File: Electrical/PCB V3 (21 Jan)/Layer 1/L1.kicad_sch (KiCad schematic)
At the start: 210 parts, among them J1 Conn_01x05, U1 LM2587S-ADJ, U2 CD74HC4067SM, U3 CD74HC4067SM, U4 XT30UPB-M, U5 113991054

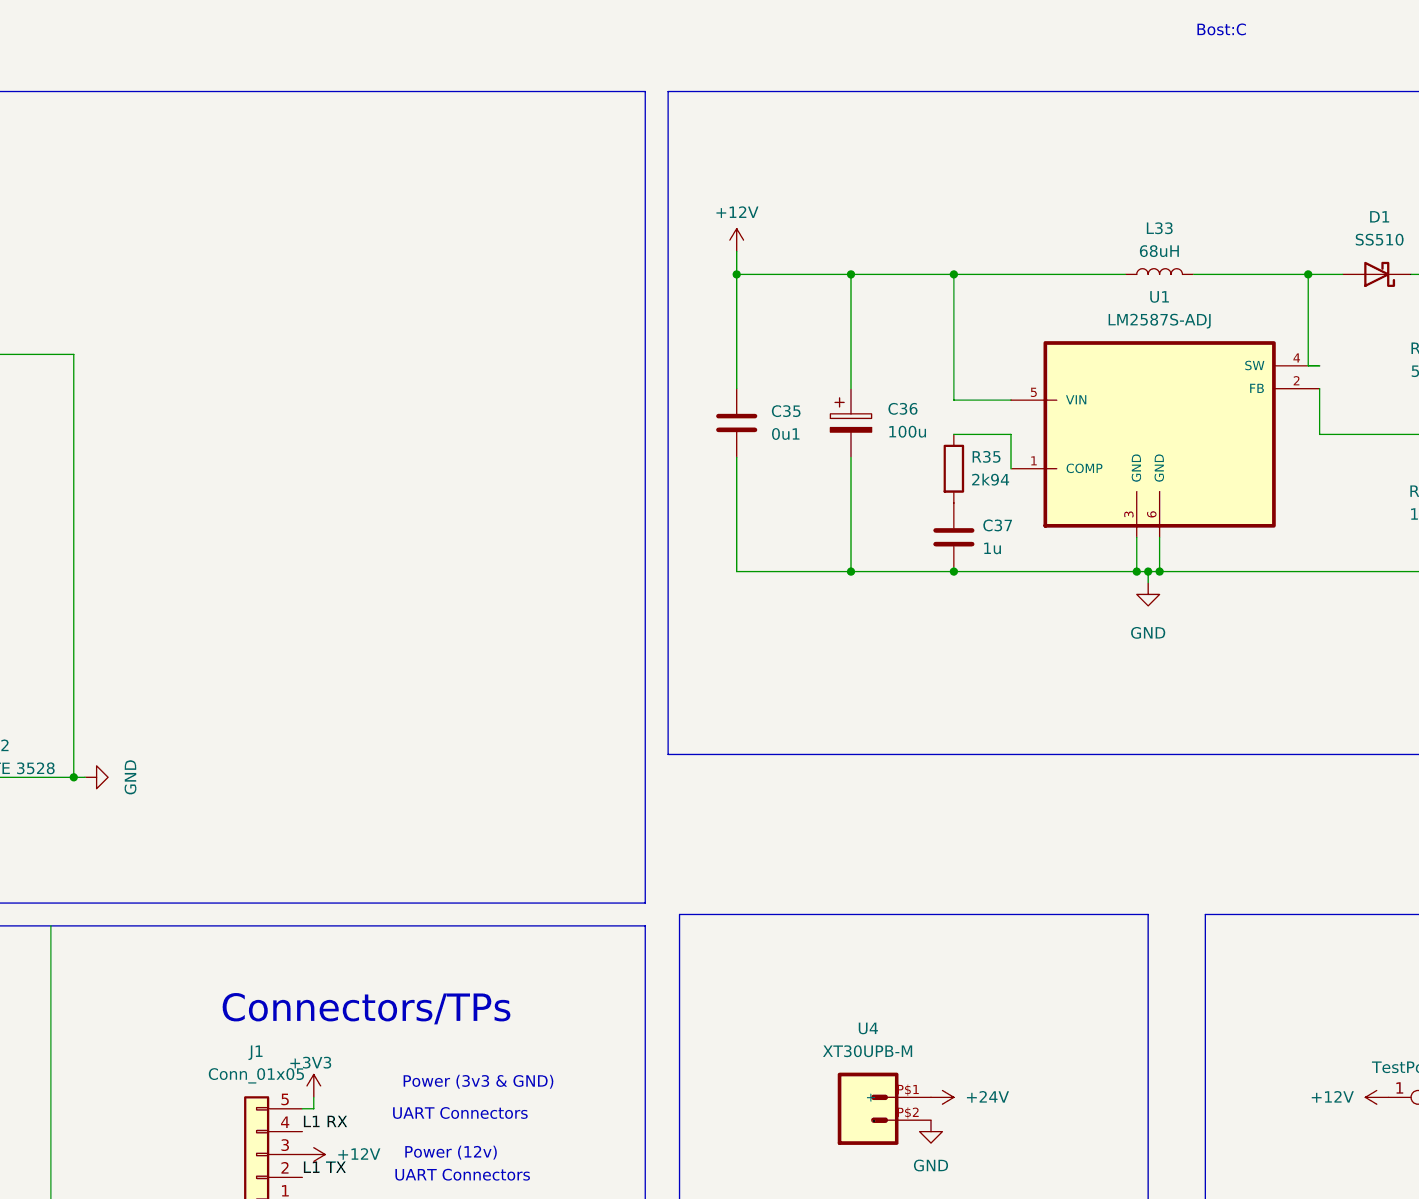
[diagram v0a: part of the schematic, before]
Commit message: redid l1 to fit new solenoid, updated l2 dxf to v6
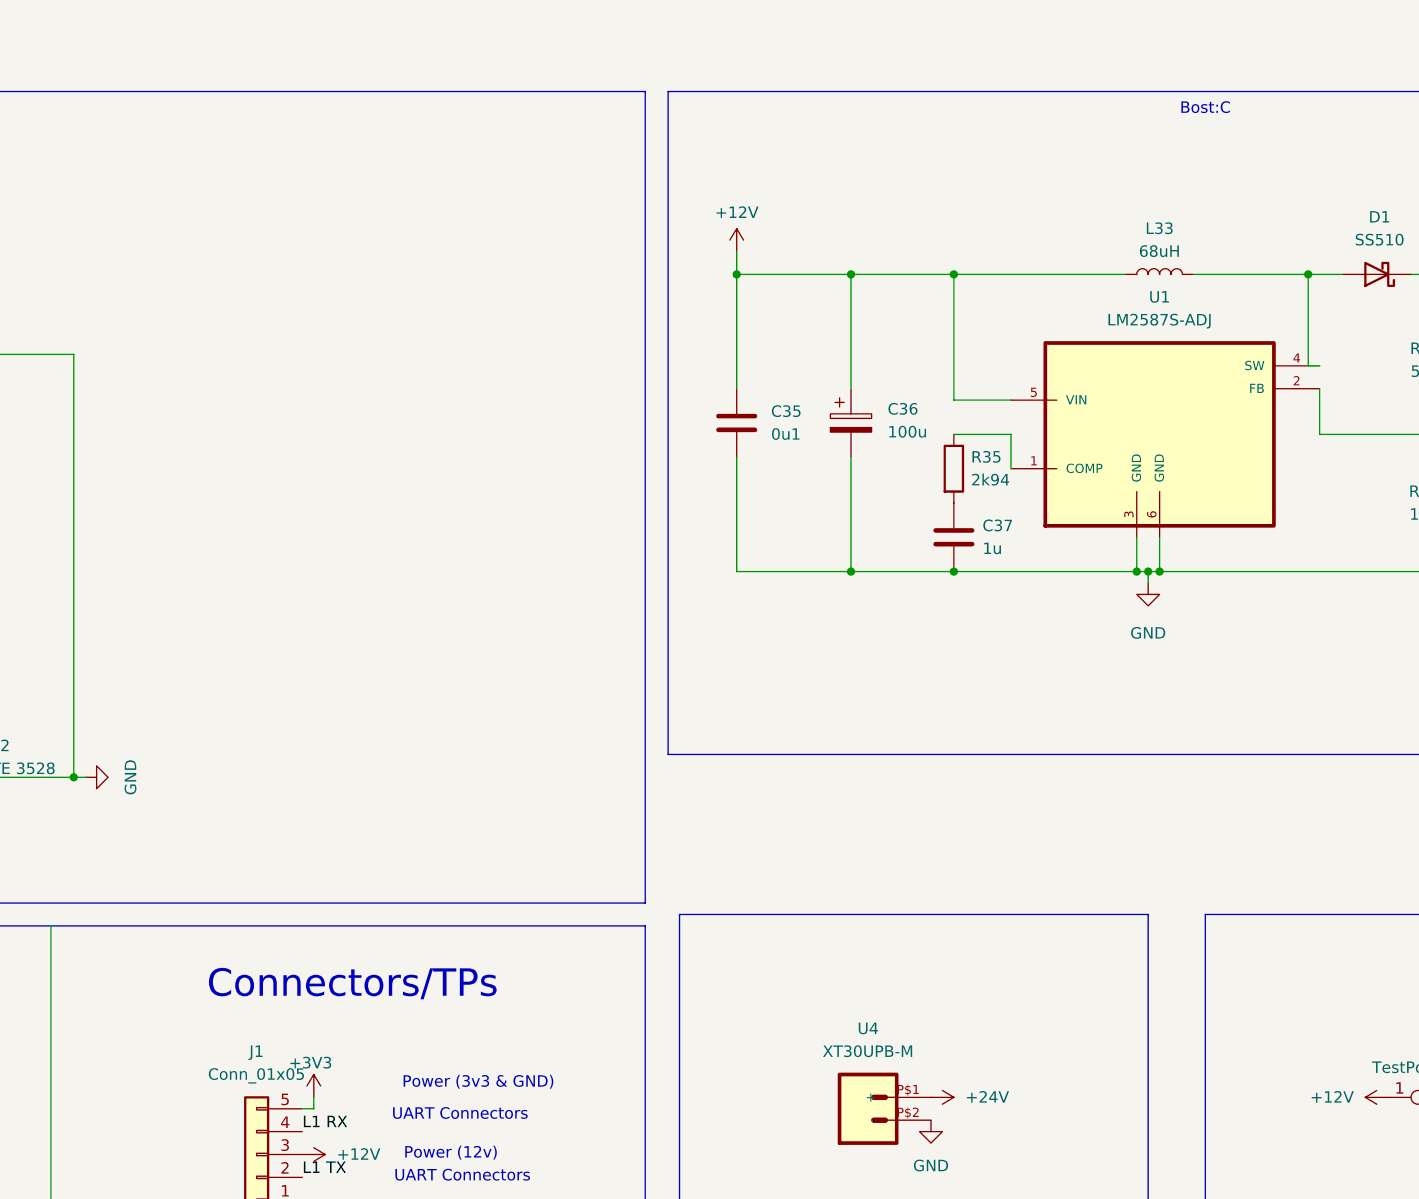
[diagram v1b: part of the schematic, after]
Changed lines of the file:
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@@
 	(text "Bost:C"
 		(exclude_from_sim no)
-		(at 462.788 17.526 0)
+		(at 461.01 26.162 0)
 		(effects
 			(font
@@
 	(text "Connectors/TPs"
 		(exclude_from_sim no)
-		(at 367.792 126.238 0)
+		(at 366.268 123.444 0)
 		(effects
 			(font
@@
 	(label "S3"
 		(at 198.12 177.8 180)
-		(fields_autoplaced yes)
 		(effects
 			(font
@@
 	(label "Mux Com (17-32)"
 		(at 247.65 176.53 270)
-		(fields_autoplaced yes)
 		(effects
 			(font
@@
 	(label "S0"
 		(at 190.5 177.8 180)
-		(fields_autoplaced yes)
 		(effects
 			(font
@@
 	(label "S2"
 		(at 270.51 177.8 180)
-		(fields_autoplaced yes)
 		(effects
 			(font
@@
 	(label "S1"
 		(at 193.04 177.8 180)
-		(fields_autoplaced yes)
 		(effects
 			(font
@@
 	(label "S0"
 		(at 265.43 177.8 180)
-		(fields_autoplaced yes)
 		(effects
 			(font
@@
 	(label "Mux Com (17-32)"
 		(at 209.55 213.36 180)
-		(fields_autoplaced yes)
 		(effects
 			(font
@@
 	(label "Mux Com (1-16)"
 		(at 209.55 215.9 180)
-		(fields_autoplaced yes)
 		(effects
 			(font
@@
 	(label "L1 RX"
 		(at 245.11 215.9 0)
-		(fields_autoplaced yes)
 		(effects
 			(font
@@
 	(label "S1"
 		(at 209.55 220.98 180)
-		(fields_autoplaced yes)
 		(effects
 			(font
@@
 	(label "S0"
 		(at 209.55 218.44 180)
-		(fields_autoplaced yes)
 		(effects
 			(font
@@
 	(label "S3"
 		(at 245.11 220.98 0)
-		(fields_autoplaced yes)
 		(effects
 			(font
@@
 	(label "S3"
 		(at 273.05 177.8 180)
-		(fields_autoplaced yes)
 		(effects
 			(font
@@
 	(label "L1 TX"
 		(at 360.68 144.78 0)
-		(fields_autoplaced yes)
 		(effects
 			(font
@@
 	(label "S1"
 		(at 267.97 177.8 180)
-		(fields_autoplaced yes)
 		(effects
 			(font
@@
 	(label "S2"
 		(at 245.11 223.52 0)
-		(fields_autoplaced yes)
 		(effects
 			(font
@@
 	(label "S2"
 		(at 195.58 177.8 180)
-		(fields_autoplaced yes)
 		(effects
 			(font
@@
 	(label "L1 RX"
 		(at 360.68 139.7 0)
-		(fields_autoplaced yes)
 		(effects
 			(font
@@
 	(label "Mux Com (1-16)"
 		(at 172.72 175.26 270)
-		(fields_autoplaced yes)
 		(effects
 			(font
@@
 	(label "L1 TX"
 		(at 245.11 213.36 0)
-		(fields_autoplaced yes)
-		(effects
-			(font
+		(effects
+			(font

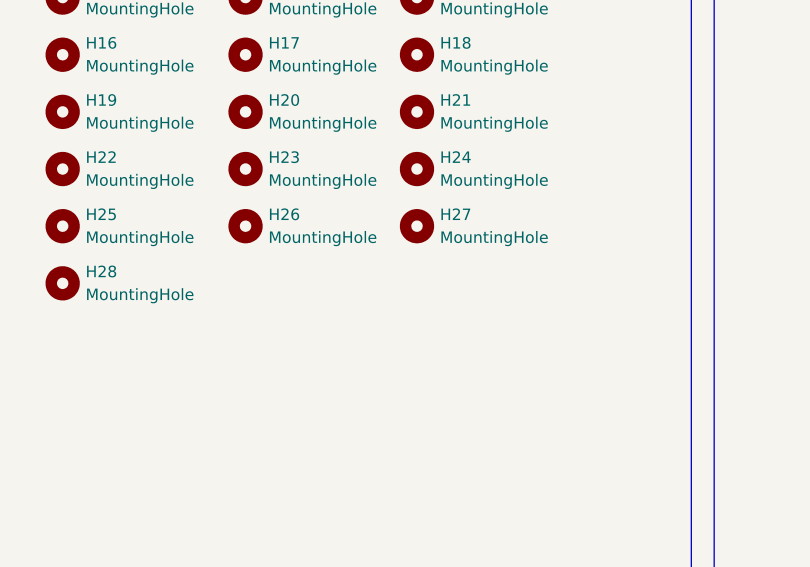
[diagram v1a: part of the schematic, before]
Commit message: fixed l1 and l3
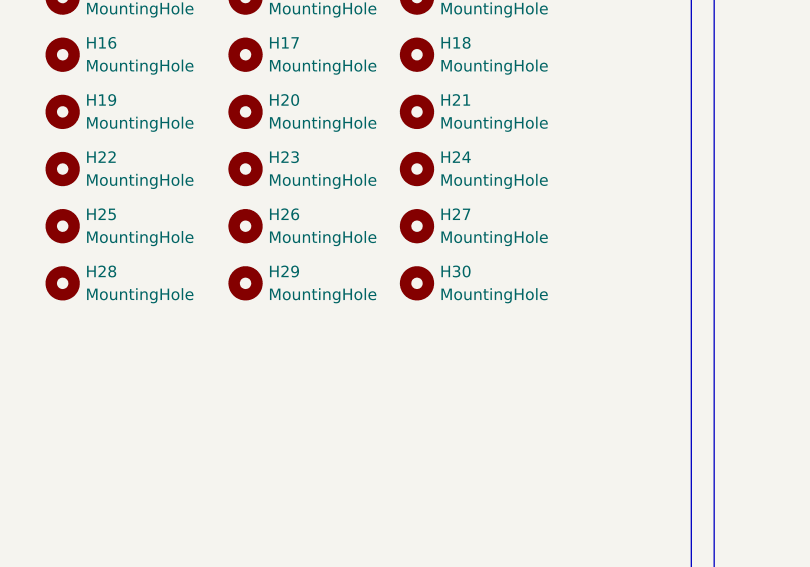
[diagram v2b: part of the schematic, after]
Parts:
- added H29, H30: MountingHole, MountingHole:MountingHole_3.2mm_M3_DIN965_Pad, symbol Mechanical:MountingHole
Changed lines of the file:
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@@
 	)
 	(symbol
+		(lib_id "Mechanical:MountingHole")
+		(at 67.31 201.93 0)
+		(unit 1)
+		(exclude_from_sim yes)
+		(in_bom no)
+		(on_board yes)
+		(dnp no)
+		(fields_autoplaced yes)
+		(property "Reference" "H29"
+			(at 69.85 200.6599 0)
+			(effects
+				(font
+					(size 1.27 1.27)
+				)
+				(justify left)
+			)
+		)
+		(property "Value" "MountingHole"
+			(at 69.85 203.1999 0)
+			(effects
+				(font
+					(size 1.27 1.27)
+				)
+				(justify left)
+			)
+		)
+		(property "Footprint" "MountingHole:MountingHole_3.2mm_M3_DIN965_Pad"
+			(at 67.31 201.93 0)
+			(effects
+				(font
+					(size 1.27 1.27)
+				)
+				(hide yes)
+			)
+		)
+		(property "Datasheet" "~"
+			(at 67.31 201.93 0)
+			(effects
+				(font
+					(size 1.27 1.27)
+				)
+				(hide yes)
+			)
+		)
+		(property "Description" "Mounting Hole without connection"
+			(at 67.31 201.93 0)
+			(effects
+				(font
+					(size 1.27 1.27)
+				)
+				(hide yes)
+			)
+		)
+		(instances
+			(project "L1"
+				(path "/9e8a7821-ee65-4356-a785-1f444d794ef4"
+					(reference "H29")
+					(unit 1)
+				)
+			)
+		)
+	)
+	(symbol
 		(lib_id "pspice:INDUCTOR")
 		(at 255.27 86.36 90)
@@
 					(unit 1)
 				)
+			)
+		)
+	)
+	(symbol
+		(lib_id "Mechanical:MountingHole")
+		(at 86.36 201.93 0)
+		(unit 1)
+		(exclude_from_sim yes)
+		(in_bom no)
+		(on_board yes)
+		(dnp no)
+		(fields_autoplaced yes)
+		(property "Reference" "H30"
+			(at 88.9 200.6599 0)
+			(effects
+				(font
+					(size 1.27 1.27)
+				)
+				(justify left)
+			)
+		)
+		(property "Value" "MountingHole"
+			(at 88.9 203.1999 0)
+			(effects
+				(font
+					(size 1.27 1.27)
+				)
+				(justify left)
+			)
+		)
+		(property "Footprint" "MountingHole:MountingHole_3.2mm_M3_DIN965_Pad"
+			(at 86.36 201.93 0)
+			(effects
+				(font
+					(size 1.27 1.27)
+				)
+				(hide yes)
+			)
+		)
+		(property "Datasheet" "~"
+			(at 86.36 201.93 0)
+			(effects
+				(font
+					(size 1.27 1.27)
+				)
+				(hide yes)
+			)
+		)
+		(property "Description" "Mounting Hole without connection"
+			(at 86.36 201.93 0)
+			(effects
+				(font
+					(size 1.27 1.27)
+				)
+				(hide yes)
+			)
+		)
+		(instances
+			(project "L1"
+				(path "/9e8a7821-ee65-4356-a785-1f444d794ef4"
+					(reference "H30")
+					(unit 1)
+				)

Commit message: fixed l1 boost, started on activation circuit
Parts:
- removed C37: 1u, Capacitor_THT:CP_Axial_L10.0mm_D6.0mm_P15.00mm_Horizontal, symbol Device:C
- removed C38: 0u1, Capacitor_THT:CP_Axial_L10.0mm_D6.0mm_P15.00mm_Horizontal, symbol Device:C
- removed D1: SS510, Capacitor_SMD:C_0603_1608Metric, symbol Device:D_Schottky
- removed R37: 1K5, Sen Robo:res0603, symbol Device:R
- added C37, C38, C41, C42, C43: 1000uF, Capacitor_THT:CP_Axial_L10.0mm_D6.0mm_P15.00mm_Horizontal, symbol Device:C_Polarized
- added C40: .68uF, Capacitor_THT:CP_Axial_L10.0mm_D6.0mm_P15.00mm_Horizontal, symbol Device:C
- added D1: D, symbol Device:D
- added D2: MBR745, Package_TO_SOT_THT:TO-220-2_Vertical, symbol Diode:MBR745
- added R38: 3k, Sen Robo:res0603, symbol Device:R
- C35: value 0u1 -> 0.1u1
- C36: value 100u -> 100uF
- C39: value 220uF -> 1000uF
- L33: value 68uH -> 33uH
- R35: value 2k94 -> 36.9K; LCSC C137748 -> C23082
- R36: value 57K -> 2K; LCSC C23082 -> C22843
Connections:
- net +24V: now also R35.1, C37.1, C38.1, C41.1, C42.1, C43.1, D2.1 (K); no longer R36.1, U4.P$1 (+)
- net GND: now also R36.2, C37.2, C38.2, C40.2, C41.2, C42.2, C43.2, D1.1 (K)
- net at U1.2 (FB): now also R35.2, R36.1; no longer R36.2
- net at U1.1 (COMP): now also R38.1; no longer R35.1
- net at L33.2, U1.4 (SW): now also D2.2 (A)
- new net: D1.2 (A), U4.P$1 (+)
- new net: C40.1, R38.2
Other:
- note added: "12V/24V Tp"
- note added: "Activation Circuit"
- note added: "Boost & Capacitors"
- note added: "To L2"
- note removed: "Bost:C"
- moved on the sheet: C35, J1, L33, R33, R34, TP2, U1, U4

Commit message: fixed l1 solenoid mosfet
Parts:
- added Q1: NMOS, symbol Simulation_SPICE:NMOS
- added R37: 3k24, Capacitor_SMD:C_0603_1608Metric, symbol Device:R
- C33, C34: value C -> .1uF
- C35: value 0.1u1 -> 0.1uF; footprint Capacitor_THT:CP_Axial_L10.0mm_D6.0mm_P15.00mm_Horizontal -> (none)
- C36, C37, C38, C39, C41, C42, C43: footprint Capacitor_THT:CP_Axial_L10.0mm_D6.0mm_P15.00mm_Horizontal -> (none)
- C40: value .68uF -> 0.68uF; footprint Capacitor_THT:CP_Axial_L10.0mm_D6.0mm_P15.00mm_Horizontal -> (none)
- D2: footprint Package_TO_SOT_THT:TO-220-2_Vertical -> (none)
- J1: footprint Connector_PinHeader_2.54mm:PinHeader_1x05_P2.54mm_Vertical -> Connector_JST:JST_EH_B5B-EH-A_1x05_P2.50mm_Vertical
- R33, R34: value R -> 3k24
- R35, R36: footprint Sen Robo:res0603 -> Capacitor_SMD:C_0603_1608Metric
- R38: value 3k -> 3K; footprint Sen Robo:res0603 -> Capacitor_SMD:C_0603_1608Metric
- TP1: value TestPoint_2Pole -> Led 3v3 & Gnd TP
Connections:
- net +24V: now also D1.2 (A), Q1.3 (S)
- net GND: now also R37.2
- net at U4.P$1 (+): now also Q1.1 (D); no longer D1.2 (A)
- net Solenoid Activation: now reaches U5.9 (D8)
- net Solenoid Activation: now also Q1.2 (G), R37.1
- no-connect marks 6 -> 5
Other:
- note added: "12V/24V TP"
- note added: "Boost & Capactiors"
- note added: "Solenoid Activation Circuit"
- note removed: "12V/24V Tp"
- note removed: "3k24"
- note removed: "Activation Circuit"
- note removed: "Boost & Capacitors"
- note removed: "LED 3v3 & Gnd TP"
- moved on the sheet: C1, C10, C11, C12, C13, C14, C15, C16, C17, C18, C19, C2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

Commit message: updated tp footprint, added library
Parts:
- C37, C38, C39, C41, C42, C43: footprint (none) -> Capacitor_THT:CP_Radial_D16.0mm_P7.50mm
- TP1: footprint Connector_PinHeader_2.54mm:PinHeader_1x02_P2.54mm_Vertical -> customTps-2-Chairs.:testpoint_2pad_2-chairs.
- TP2: footprint Connector_PinHeader_2.54mm:PinHeader_1x02_P2.54mm_Vertical -> TestPoint:TestPoint_2Pads_Pitch2.54mm_Drill0.8mm
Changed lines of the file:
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@@
 			)
 		)
-		(property "Footprint" ""
+		(property "Footprint" "Capacitor_THT:CP_Radial_D16.0mm_P7.50mm"
 			(at 535.6352 77.47 0)
 			(effects
@@
 			)
 		)
-		(property "Footprint" ""
+		(property "Footprint" "Capacitor_THT:CP_Radial_D16.0mm_P7.50mm"
 			(at 520.3952 77.47 0)
 			(effects
@@
 			)
 		)
-		(property "Footprint" ""
+		(property "Footprint" "Capacitor_THT:CP_Radial_D16.0mm_P7.50mm"
 			(at 505.1552 77.47 0)
 			(effects
@@
 			)
 		)
-		(property "Footprint" ""
+		(property "Footprint" "Capacitor_THT:CP_Radial_D16.0mm_P7.50mm"
 			(at 512.7752 77.47 0)
 			(effects
@@
 			)
 		)
-		(property "Footprint" "Connector_PinHeader_2.54mm:PinHeader_1x02_P2.54mm_Vertical"
+		(property "Footprint" "TestPoint:TestPoint_2Pads_Pitch2.54mm_Drill0.8mm"
 			(at 361.95 200.66 0)
 			(effects
@@
 			)
 		)
-		(property "Footprint" ""
+		(property "Footprint" "Capacitor_THT:CP_Radial_D16.0mm_P7.50mm"
 			(at 497.5352 77.47 0)
 			(effects
@@
 			)
 		)
-		(property "Footprint" ""
+		(property "Footprint" "Capacitor_THT:CP_Radial_D16.0mm_P7.50mm"
 			(at 528.0152 77.47 0)
 			(effects
@@
 			)
 		)
-		(property "Footprint" "Connector_PinHeader_2.54mm:PinHeader_1x02_P2.54mm_Vertical"
+		(property "Footprint" "customTps-2-Chairs.:testpoint_2pad_2-chairs."
 			(at 87.63 52.07 0)
 			(effects

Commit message: updated custom testpoint
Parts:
- TP1: footprint customTps-2-Chairs.:testpoint_2pad_2-chairs. -> customTps-2-Chairs:testpoint_2pad_2-chairs.
- TP2: footprint TestPoint:TestPoint_2Pads_Pitch2.54mm_Drill0.8mm -> customTps-2-Chairs:testpoint_2pad_2-chairs.
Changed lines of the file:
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@@
 			)
 		)
-		(property "Footprint" "TestPoint:TestPoint_2Pads_Pitch2.54mm_Drill0.8mm"
+		(property "Footprint" "customTps-2-Chairs:testpoint_2pad_2-chairs."
 			(at 361.95 200.66 0)
 			(effects
@@
 			)
 		)
-		(property "Footprint" "customTps-2-Chairs.:testpoint_2pad_2-chairs."
+		(property "Footprint" "customTps-2-Chairs:testpoint_2pad_2-chairs."
 			(at 87.63 52.07 0)
 			(effects

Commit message: somewhat did boost pcb. pending improvements
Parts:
- C35, C40: footprint (none) -> Capacitor_SMD:C_0603_1608Metric
- C36: footprint (none) -> Capacitor_THT:CP_Radial_D8.0mm_P3.50mm
- D1: footprint (none) -> Diode_SMD:D_0603_1608Metric
- D2: footprint (none) -> Package_TO_SOT_THT:TO-220-2_Vertical
- Q1: footprint (none) -> Package_TO_SOT_THT:TO-220-3_Vertical
- U1: footprint layer2v3:VREG_LM5017MR_NOPB -> LM2587S-ADJ:VREG_TPS79625KTTR
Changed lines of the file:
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@@
 			)
 		)
-		(property "Footprint" ""
+		(property "Footprint" "Package_TO_SOT_THT:TO-220-2_Vertical"
 			(at 482.6 48.895 0)
 			(effects
@@
 			)
 		)
-		(property "Footprint" ""
+		(property "Footprint" "Package_TO_SOT_THT:TO-220-3_Vertical"
 			(at 513.08 179.07 0)
 			(effects
@@
 			)
 		)
-		(property "Footprint" ""
+		(property "Footprint" "Capacitor_THT:CP_Radial_D8.0mm_P3.50mm"
 			(at 402.2852 77.47 0)
 			(effects
@@
 			)
 		)
-		(property "Datasheet" "https://www.mouser.com/ProductDetail/Nichicon/UPL1H101MPH?qs=46TSnLWiWr6vwJWSAA6xeQ%3D%3D"
+		(property "Datasheet" "https://www.mouser.com/ProductDetail/Nichicon/UPS1H101MPD1TD?qs=I4WtNW3K5bKJX9mnjMCynA%3D%3D"
 			(at 401.32 73.66 0)
 			(effects
@@
 			)
 		)
-		(property "Footprint" "layer2v3:VREG_LM5017MR_NOPB"
+		(property "Footprint" "LM2587S-ADJ:VREG_TPS79625KTTR"
 			(at 450.85 72.39 0)
 			(effects
@@
 			)
 		)
-		(property "Footprint" ""
+		(property "Footprint" "Diode_SMD:D_0603_1608Metric"
 			(at 516.89 176.53 0)
 			(effects
@@
 			)
 		)
-		(property "Footprint" ""
+		(property "Footprint" "Capacitor_SMD:C_0603_1608Metric"
 			(at 426.4152 92.71 0)
 			(effects
@@
 			)
 		)
-		(property "Datasheet" "~"
+		(property "Datasheet" "https://www.mouser.sg/ProductDetail/Vishay-Vitramon/VJ0603AR68BXACW1BC?qs=RVW9LZWsH%252BhTCb7z9MQClQ%3D%3D"
 			(at 425.45 88.9 0)
 			(effects
@@
 			)
 		)
-		(property "Footprint" ""
+		(property "Footprint" "Capacitor_SMD:C_0603_1608Metric"
 			(at 416.2552 77.47 0)
 			(effects
